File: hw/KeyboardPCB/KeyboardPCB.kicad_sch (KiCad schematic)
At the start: 176 parts, among them IC1 TPS2113ADRBR, IC2 BGM220PC22HNA2R, J1 USB_B_Micro, J2 Conn_01x05_Pin, J3 Conn_01x06_Pin, K1 KEYSW, K10 KEYSW, K11 KEYSW, K12 KEYSW, K13 KEYSW, K14 KEYSW, K15 KEYSW, K16 KEYSW, K17 KEYSW, K18 KEYSW, K19 KEYSW, K2 KEYSW, K21 KEYSW, K22 KEYSW, K23 KEYSW, K24 KEYSW, K26 KEYSW, K27 KEYSW, K28 KEYSW, K29 KEYSW, K3 KEYSW, K30 KEYSW, K31 KEYSW, K32 KEYSW, K33 KEYSW, K34 KEYSW, K36 KEYSW, K37 KEYSW, K38 KEYSW, K39 KEYSW, K4 KEYSW, K41 KEYSW, K42 KEYSW, K43 KEYSW, K44 KEYSW, K46 KEYSW, K47 KEYSW, K48 KEYSW, K49 KEYSW, K5 KEYSW, K50 KEYSW, K51 KEYSW, K52 KEYSW, K53 KEYSW, K54 KEYSW, K55 KEYSW, K56 KEYSW, K57 KEYSW, K58 KEYSW, K59 KEYSW, K6 KEYSW, K60 KEYSW, K61 KEYSW, K62 KEYSW, K64 KEYSW, K65 KEYSW, K66 KEYSW, K67 KEYSW, K68 KEYSW, K69 KEYSW, K7 KEYSW, K8 KEYSW, SW1 SW_Push, U1 TM4C123GH6PMI7, U2 TPS73633DBV, U3 Adafruit ST7735R, X2 16MHz

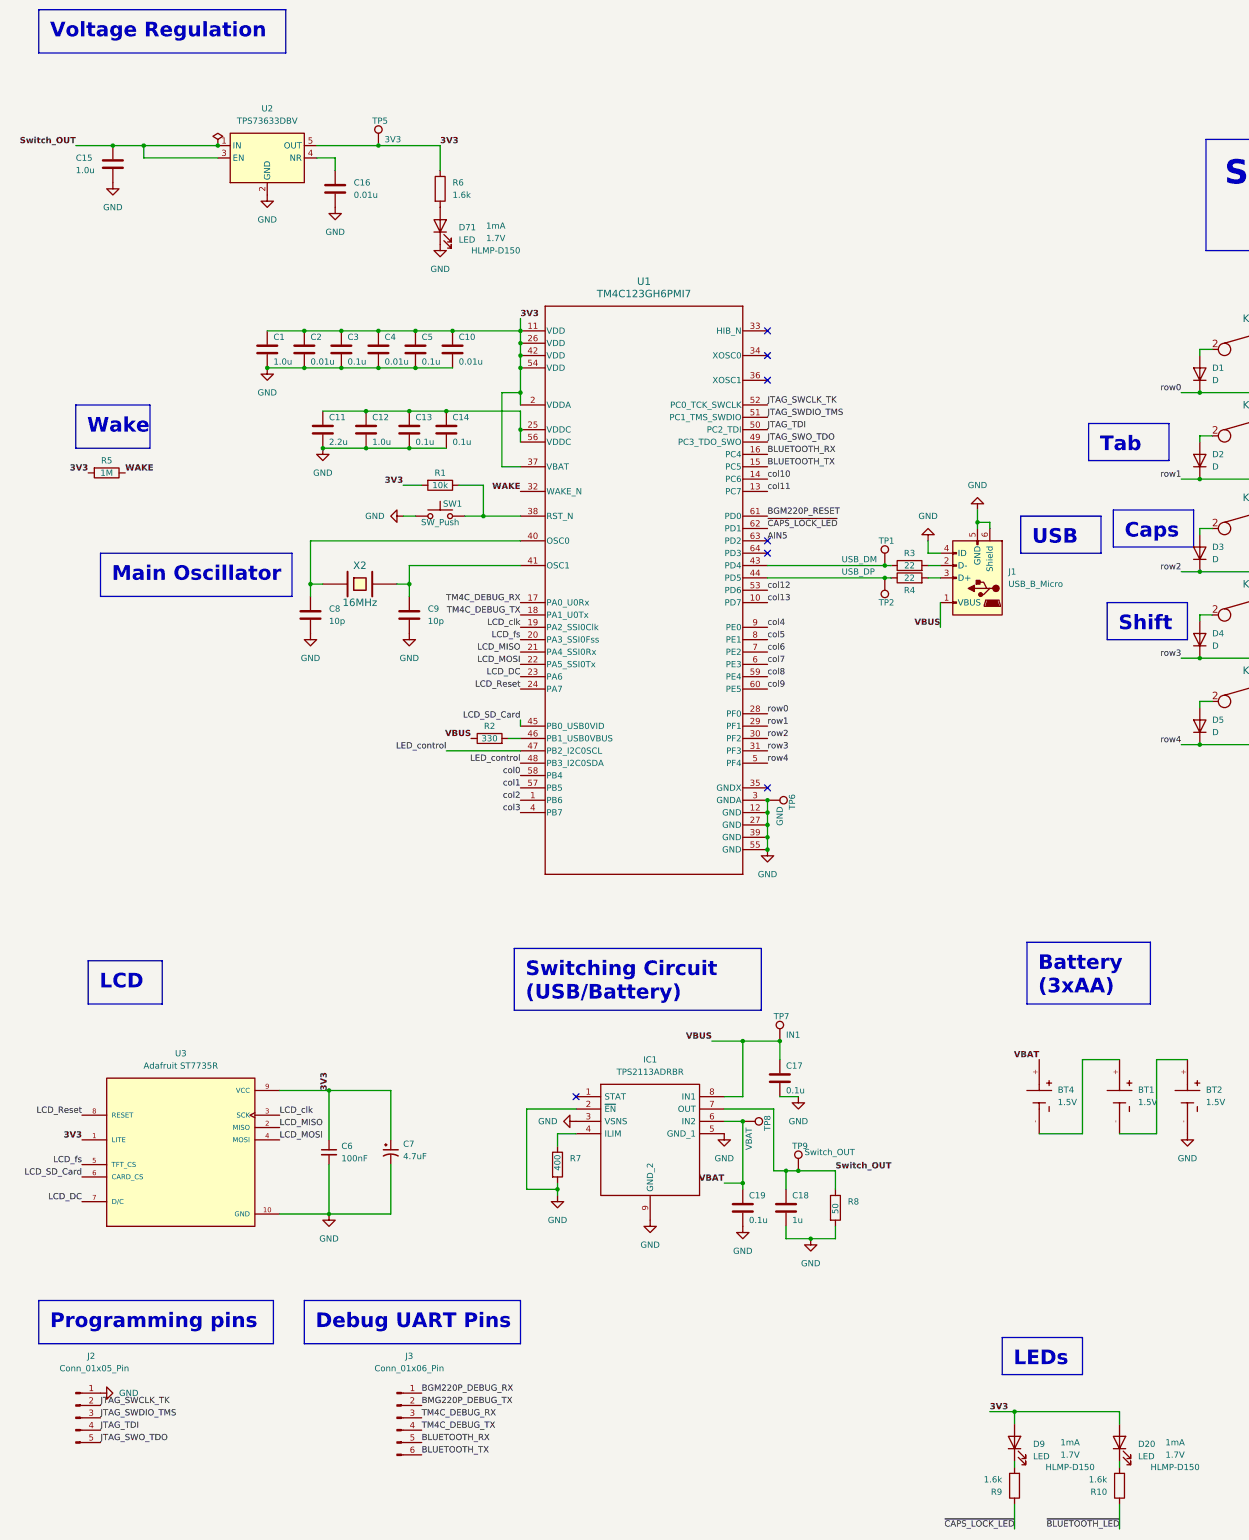
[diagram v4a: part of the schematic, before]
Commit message: Verified TM4C pin #s and important pins, MOSC, and caps
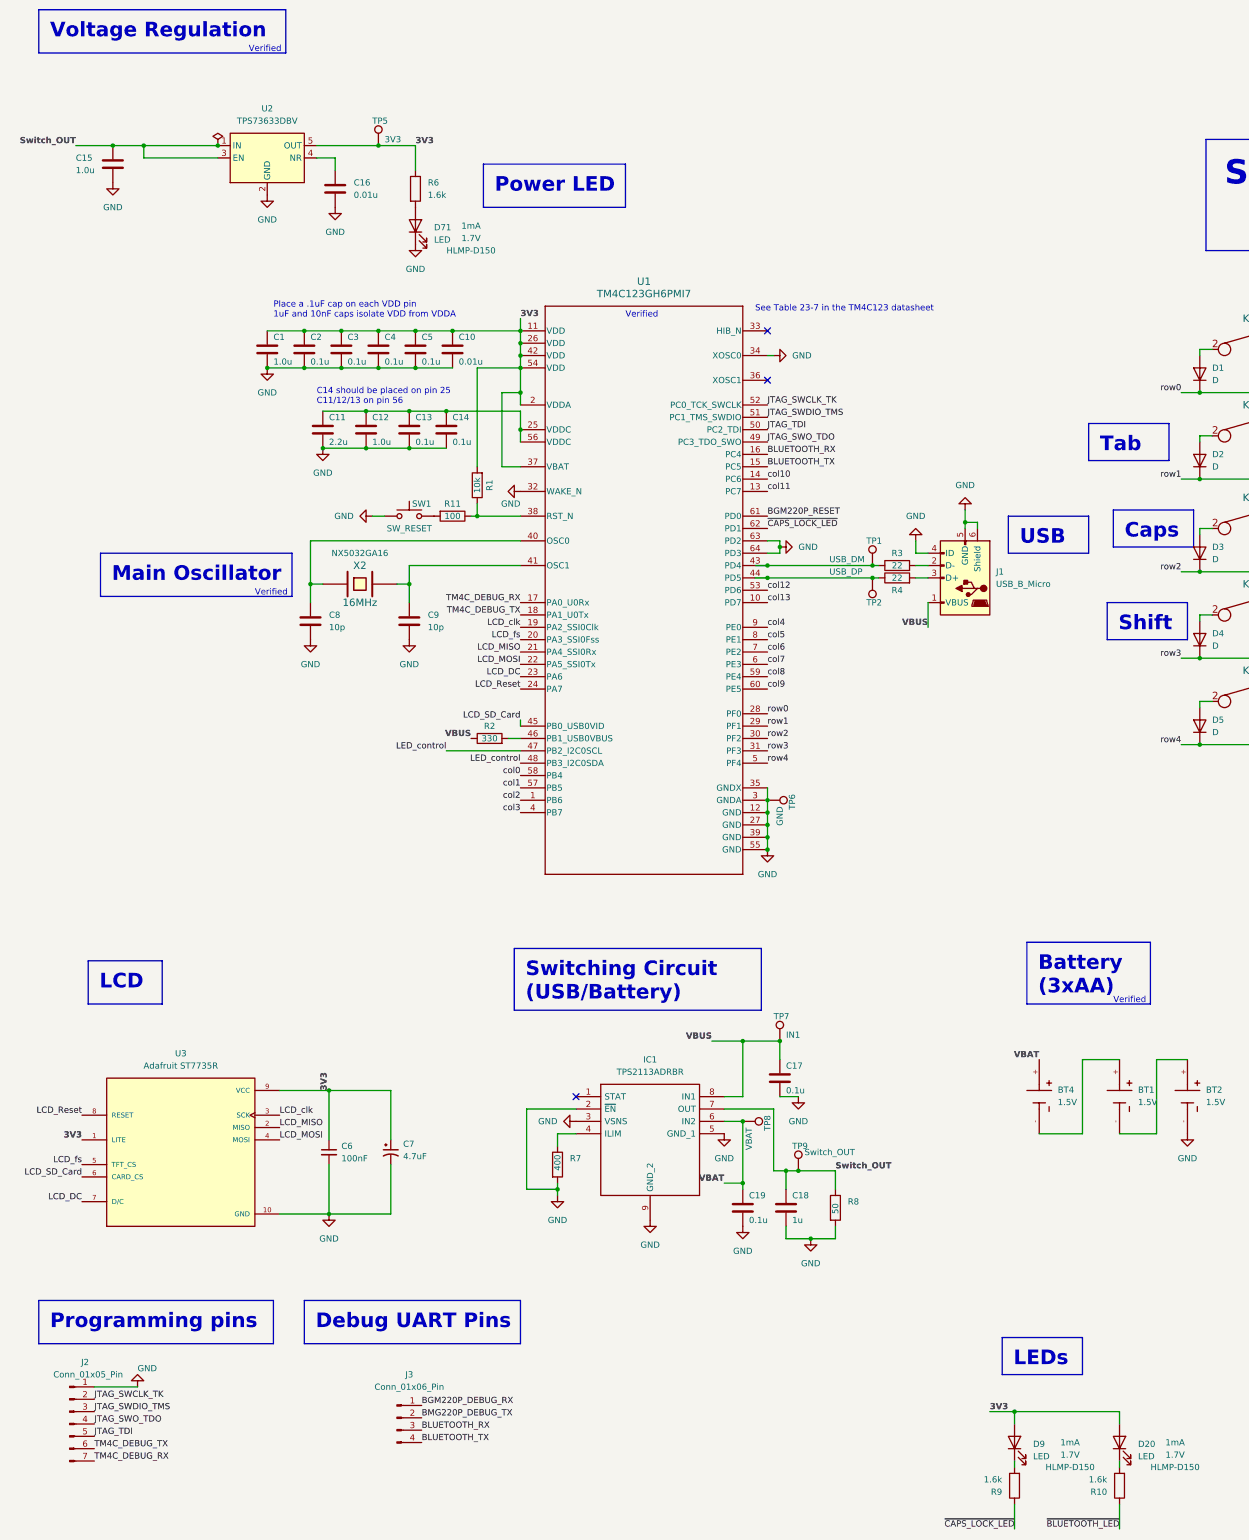
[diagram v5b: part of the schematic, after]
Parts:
- removed R5: 1M, Resistor_SMD:R_0402_1005Metric, symbol Device:R
- added R11: 100, Resistor_SMD:R_0402_1005Metric, symbol Device:R
- C2, C4: value 0.01u -> 0.1u
- J2: symbol Connector:Conn_01x05_Pin -> Connector:Conn_01x07_Pin
- J3: symbol Connector:Conn_01x06_Pin -> Connector:Conn_01x04_Pin
- SW1: value SW_Push -> SW_RESET
- U1: footprint TM4C123GH6PM:PM0064A_L -> TM4C:QFP50P1200X1200X160-64N
- X2: P/N (none) -> NX5032GA16
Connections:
- net AIN5 is gone; now on net GND: U1.63 (PD2)
- net WAKE is gone; now on net GND: U1.32 (WAKE_N)
- net BLUETOOTH_RX: now also J3.3 (Pin_3); no longer J3.5 (Pin_5)
- net BLUETOOTH_TX: now also J3.4 (Pin_4); no longer J3.6 (Pin_6)
- net GND: now also U1.34 (XOSC0), U1.35 (GNDX), U1.64 (PD3)
- net JTAG_SWO_TDO: now also J2.4 (Pin_4); no longer J2.5 (Pin_5)
- net JTAG_TDI: now also J2.5 (Pin_5); no longer J2.4 (Pin_4)
- net TM4C_DEBUG_RX: now also J2.7 (Pin_7); no longer J3.3 (Pin_3)
- net TM4C_DEBUG_TX: now also J2.6 (Pin_6); no longer J3.4 (Pin_4)
- net at R1.1, U1.38 (RST_N): now also R11.1; no longer SW1.2
- new net: R11.2, SW1.2
- no-connect marks 26 -> 22
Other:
- note added: "C14 should be placed on pin 25 C11/12/13 on pin 56"
- note added: "Place a .1uF cap on each VDD pin 1uF and 10nF caps isolate VDD from VDDA"
- note added: "See Table 23-7 in the TM4C123 datasheet"
- note added: "Verified"
- moved on the sheet: C8, C9, D71, J1, R1, R3, R4, R6, SW1, TP1, TP2

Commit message: Verified LCD, power mux, JTAG, USB, and switch matrix
Also changed the switch matrix to use hotswap footprints
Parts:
- removed C18: 1u, Capacitor_SMD:C_0603_1608Metric_Pad1.08x0.95mm_HandSolder, symbol Device:C
- removed R8: 50, Resistor_SMD:R_0402_1005Metric, symbol Device:R
- removed TP9: Switch_OUT, TestPoint:TestPoint_Pad_2.5x2.5mm, symbol Connector:TestPoint
- added TP3: Switch_OUT, TestPoint:TestPoint_Pad_2.5x2.5mm, symbol Connector:TestPoint
- J2: value Conn_01x05_Pin -> Conn_01x07_Pin
- J3: symbol Connector:Conn_01x04_Pin -> Connector:Conn_01x06_Pin
- K1: footprint keebs.pretty-master:Mx_Alps_100 -> MX_Hotswap:MX-Hotswap-1U
- K10: renamed from K46; footprint keebs.pretty-master:Mx_Alps_100 -> MX_Hotswap:MX-Hotswap-1U
- K11: renamed from K51; footprint keebs.pretty-master:Mx_Alps_100 -> MX_Hotswap:MX-Hotswap-1U
- K12: renamed from K56; footprint keebs.pretty-master:Mx_Alps_100 -> MX_Hotswap:MX-Hotswap-1U
- K13: renamed from K61; footprint keebs.pretty-master:Mx_Alps_100 -> MX_Hotswap:MX-Hotswap-1U
- K14: renamed from K66; footprint keebs.pretty-master:Mx_Alps_200 -> MX_Hotswap:MX-Hotswap-2U
- K15: renamed from K2; footprint keebs.pretty-master:Mx_Alps_150 -> MX_Hotswap:MX-Hotswap-1.5U
- K16: renamed from K7; footprint keebs.pretty-master:Mx_Alps_100 -> MX_Hotswap:MX-Hotswap-1U
- K17: renamed from K12; footprint keebs.pretty-master:Mx_Alps_100 -> MX_Hotswap:MX-Hotswap-1U
- K18: renamed from K17; footprint keebs.pretty-master:Mx_Alps_100 -> MX_Hotswap:MX-Hotswap-1U
- K19: renamed from K22; footprint keebs.pretty-master:Mx_Alps_100 -> MX_Hotswap:MX-Hotswap-1U
- K2: renamed from K6; footprint keebs.pretty-master:Mx_Alps_100 -> MX_Hotswap:MX-Hotswap-1U
- K20: renamed from K27; footprint keebs.pretty-master:Mx_Alps_100 -> MX_Hotswap:MX-Hotswap-1U
- K21: renamed from K32; footprint keebs.pretty-master:Mx_Alps_100 -> MX_Hotswap:MX-Hotswap-1U
- K22: renamed from K37; footprint keebs.pretty-master:Mx_Alps_100 -> MX_Hotswap:MX-Hotswap-1U
- K23: renamed from K42; footprint keebs.pretty-master:Mx_Alps_100 -> MX_Hotswap:MX-Hotswap-1U
- K24: renamed from K47; footprint keebs.pretty-master:Mx_Alps_100 -> MX_Hotswap:MX-Hotswap-1U
- K25: renamed from K52; footprint keebs.pretty-master:Mx_Alps_100 -> MX_Hotswap:MX-Hotswap-1U
- K26: renamed from K57; footprint keebs.pretty-master:Mx_Alps_100 -> MX_Hotswap:MX-Hotswap-1U
- K27: renamed from K62; footprint keebs.pretty-master:Mx_Alps_100 -> MX_Hotswap:MX-Hotswap-1U
- K28: renamed from K67; footprint keebs.pretty-master:Mx_Alps_150 -> MX_Hotswap:MX-Hotswap-1.5U
- K29: renamed from K3; footprint keebs.pretty-master:Mx_Alps_175 -> MX_Hotswap:MX-Hotswap-1.75U
- K3: renamed from K11; footprint keebs.pretty-master:Mx_Alps_100 -> MX_Hotswap:MX-Hotswap-1U
- K30: renamed from K8; footprint keebs.pretty-master:Mx_Alps_100 -> MX_Hotswap:MX-Hotswap-1U
- K31: renamed from K13; footprint keebs.pretty-master:Mx_Alps_100 -> MX_Hotswap:MX-Hotswap-1U
- K32: renamed from K18; footprint keebs.pretty-master:Mx_Alps_100 -> MX_Hotswap:MX-Hotswap-1U
- K33: renamed from K23; footprint keebs.pretty-master:Mx_Alps_100 -> MX_Hotswap:MX-Hotswap-1U
- K34: renamed from K28; footprint keebs.pretty-master:Mx_Alps_100 -> MX_Hotswap:MX-Hotswap-1U
- K35: renamed from K33; footprint keebs.pretty-master:Mx_Alps_100 -> MX_Hotswap:MX-Hotswap-1U
- K36: renamed from K38; footprint keebs.pretty-master:Mx_Alps_100 -> MX_Hotswap:MX-Hotswap-1U
- K37: renamed from K43; footprint keebs.pretty-master:Mx_Alps_100 -> MX_Hotswap:MX-Hotswap-1U
- K38: renamed from K48; footprint keebs.pretty-master:Mx_Alps_100 -> MX_Hotswap:MX-Hotswap-1U
- K39: renamed from K53; footprint keebs.pretty-master:Mx_Alps_100 -> MX_Hotswap:MX-Hotswap-1U
- K4: renamed from K16; footprint keebs.pretty-master:Mx_Alps_100 -> MX_Hotswap:MX-Hotswap-1U
- K40: renamed from K58; footprint keebs.pretty-master:Mx_Alps_100 -> MX_Hotswap:MX-Hotswap-1U
- K41: renamed from K68; footprint keebs.pretty-master:Mx_Alps_225 -> MX_Hotswap:MX-Hotswap-2.25U
- K42: renamed from K4; footprint keebs.pretty-master:Mx_Alps_225 -> MX_Hotswap:MX-Hotswap-2.25U
- K43: renamed from K14; footprint keebs.pretty-master:Mx_Alps_100 -> MX_Hotswap:MX-Hotswap-1U
- K44: renamed from K19; footprint keebs.pretty-master:Mx_Alps_100 -> MX_Hotswap:MX-Hotswap-1U
- K45: renamed from K24; footprint keebs.pretty-master:Mx_Alps_100 -> MX_Hotswap:MX-Hotswap-1U
- K46: renamed from K29; footprint keebs.pretty-master:Mx_Alps_100 -> MX_Hotswap:MX-Hotswap-1U
- K47: renamed from K34; footprint keebs.pretty-master:Mx_Alps_100 -> MX_Hotswap:MX-Hotswap-1U
- K48: renamed from K39; footprint keebs.pretty-master:Mx_Alps_100 -> MX_Hotswap:MX-Hotswap-1U
- K49: renamed from K44; footprint keebs.pretty-master:Mx_Alps_100 -> MX_Hotswap:MX-Hotswap-1U
- K5: renamed from K21; footprint keebs.pretty-master:Mx_Alps_100 -> MX_Hotswap:MX-Hotswap-1U
- K50: renamed from K49; footprint keebs.pretty-master:Mx_Alps_100 -> MX_Hotswap:MX-Hotswap-1U
- K51: renamed from K54; footprint keebs.pretty-master:Mx_Alps_100 -> MX_Hotswap:MX-Hotswap-1U
- K52: renamed from K59; footprint keebs.pretty-master:Mx_Alps_100 -> MX_Hotswap:MX-Hotswap-1U
- K53: renamed from K64; footprint keebs.pretty-master:Mx_Alps_150 -> MX_Hotswap:MX-Hotswap-1.5U
- K54: renamed from K69; footprint keebs.pretty-master:Mx_Alps_125 -> MX_Hotswap:MX-Hotswap-1.25U
- K55: renamed from K5; footprint keebs.pretty-master:Mx_Alps_125 -> MX_Hotswap:MX-Hotswap-1.25U
- K56: renamed from K10; footprint keebs.pretty-master:Mx_Alps_125 -> MX_Hotswap:MX-Hotswap-1.25U
- K57: renamed from K15; footprint keebs.pretty-master:Mx_Alps_125 -> MX_Hotswap:MX-Hotswap-1.25U
- K58: renamed from K30; footprint keebs.pretty-master:Mx_Alps_625 -> MX_Hotswap:MX-Hotswap-6.25U
- K59: renamed from K50; footprint keebs.pretty-master:Mx_Alps_125 -> MX_Hotswap:MX-Hotswap-1.25U
- K6: renamed from K26; footprint keebs.pretty-master:Mx_Alps_100 -> MX_Hotswap:MX-Hotswap-1U
- K60: renamed from K55; footprint keebs.pretty-master:Mx_Alps_125 -> MX_Hotswap:MX-Hotswap-1.25U
- K61: renamed from K60; footprint keebs.pretty-master:Mx_Alps_125 -> MX_Hotswap:MX-Hotswap-1.25U
- K62: renamed from K65; footprint keebs.pretty-master:Mx_Alps_125 -> MX_Hotswap:MX-Hotswap-1.25U
- K7: renamed from K31; footprint keebs.pretty-master:Mx_Alps_100 -> MX_Hotswap:MX-Hotswap-1U
- K8: renamed from K36; footprint keebs.pretty-master:Mx_Alps_100 -> MX_Hotswap:MX-Hotswap-1U
- K9: renamed from K41; footprint keebs.pretty-master:Mx_Alps_100 -> MX_Hotswap:MX-Hotswap-1U
- R7: value 400 -> 750
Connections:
- net 3V3: now also J2.5 (Pin_5)
- net GND: now also J2.7 (Pin_7); no longer J1.4 (ID), J2.1 (Pin_1)
- net JTAG_SWDIO_TMS: now also J2.2 (Pin_2); no longer J2.3 (Pin_3)
- net JTAG_SWO_TDO: now also J2.3 (Pin_3); no longer J2.4 (Pin_4)
- net JTAG_TDI: now also J2.4 (Pin_4); no longer J2.5 (Pin_5)
- net Switch_OUT: now also TP3.1
- net TM4C_DEBUG_RX: now also J3.6 (Pin_6); no longer J2.7 (Pin_7)
- net TM4C_DEBUG_TX: now also J3.5 (Pin_5); no longer J2.6 (Pin_6)
- net row0: now also D1.2 (A), D11.2 (A), D16.2 (A), D21.2 (A), D26.2 (A), D31.2 (A), D36.2 (A), D41.2 (A), D46.2 (A), D51.2 (A), D56.2 (A), D6.2 (A), D61.2 (A), D66.2 (A); no longer D1.1 (K), D11.1 (K), D16.1 (K), D21.1 (K), D26.1 (K), D31.1 (K), D36.1 (K), D41.1 (K), D46.1 (K), D51.1 (K), D56.1 (K), D6.1 (K), D61.1 (K), D66.1 (K)
- net row1: now also D12.2 (A), D17.2 (A), D2.2 (A), D22.2 (A), D27.2 (A), D32.2 (A), D37.2 (A), D42.2 (A), D47.2 (A), D52.2 (A), D57.2 (A), D62.2 (A), D67.2 (A), D7.2 (A); no longer D12.1 (K), D17.1 (K), D2.1 (K), D22.1 (K), D27.1 (K), D32.1 (K), D37.1 (K), D42.1 (K), D47.1 (K), D52.1 (K), D57.1 (K), D62.1 (K), D67.1 (K), D7.1 (K)
- net row2: now also D13.2 (A), D18.2 (A), D23.2 (A), D28.2 (A), D3.2 (A), D33.2 (A), D38.2 (A), D43.2 (A), D48.2 (A), D53.2 (A), D58.2 (A), D68.2 (A), D8.2 (A); no longer D13.1 (K), D18.1 (K), D23.1 (K), D28.1 (K), D3.1 (K), D33.1 (K), D38.1 (K), D43.1 (K), D48.1 (K), D53.1 (K), D58.1 (K), D68.1 (K), D8.1 (K)
- net row3: now also D14.2 (A), D19.2 (A), D24.2 (A), D29.2 (A), D34.2 (A), D39.2 (A), D4.2 (A), D44.2 (A), D49.2 (A), D54.2 (A), D59.2 (A), D64.2 (A), D69.2 (A); no longer D14.1 (K), D19.1 (K), D24.1 (K), D29.1 (K), D34.1 (K), D39.1 (K), D4.1 (K), D44.1 (K), D49.1 (K), D54.1 (K), D59.1 (K), D64.1 (K), D69.1 (K)
- net row4: now also D10.2 (A), D15.2 (A), D30.2 (A), D5.2 (A), D50.2 (A), D55.2 (A), D60.2 (A), D65.2 (A); no longer D10.1 (K), D15.1 (K), D30.1 (K), D5.1 (K), D50.1 (K), D55.1 (K), D60.1 (K), D65.1 (K)
- net at K51.2: now also D54.1 (K); no longer D54.2 (A)
- net at K11.2: now also D51.1 (K); no longer D51.2 (A)
- net at K8.2: now also D36.1 (K); no longer D36.2 (A)
- net at K7.2: now also D31.1 (K); no longer D31.2 (A)
- net at K18.2: now also D17.1 (K); no longer D17.2 (A)
- net at K30.2: now also D8.1 (K); no longer D8.2 (A)
- net at K61.2: now also D60.1 (K); no longer D60.2 (A)
- net at K59.2: now also D50.1 (K); no longer D50.2 (A)
- net at K27.2: now also D62.1 (K); no longer D62.2 (A)
- net at K21.2: now also D32.1 (K); no longer D32.2 (A)
- net at K40.2: now also D58.1 (K); no longer D58.2 (A)
- net at K2.2: now also D6.1 (K); no longer D6.2 (A)
- net at K17.2: now also D12.1 (K); no longer D12.2 (A)
- net at K20.2: now also D27.1 (K); no longer D27.2 (A)
- net at K49.2: now also D44.1 (K); no longer D44.2 (A)
- net at K48.2: now also D39.1 (K); no longer D39.2 (A)
- net at K54.2: now also D69.1 (K); no longer D69.2 (A)
- net at K10.2: now also D46.1 (K); no longer D46.2 (A)
- net at K52.2: now also D59.1 (K); no longer D59.2 (A)
- net at K58.2: now also D30.1 (K); no longer D30.2 (A)
- net at K36.2: now also D38.1 (K); no longer D38.2 (A)
- net at K4.2: now also D16.1 (K); no longer D16.2 (A)
- net at K31.2: now also D13.1 (K); no longer D13.2 (A)
- net at K57.2: now also D15.1 (K); no longer D15.2 (A)
- net at K37.2: now also D43.1 (K); no longer D43.2 (A)
- net at K1.2: now also D1.1 (K); no longer D1.2 (A)
- net at K56.2: now also D10.1 (K); no longer D10.2 (A)
- net at K9.2: now also D41.1 (K); no longer D41.2 (A)
- net at K62.2: now also D65.1 (K); no longer D65.2 (A)
- net at K42.2: now also D4.1 (K); no longer D4.2 (A)
- net at K33.2: now also D23.1 (K); no longer D23.2 (A)
- net at K41.2: now also D68.1 (K); no longer D68.2 (A)
- net at K28.2: now also D67.1 (K); no longer D67.2 (A)
- net at K35.2: now also D33.1 (K); no longer D33.2 (A)
- net at K55.2: now also D5.1 (K); no longer D5.2 (A)
- net at K43.2: now also D14.1 (K); no longer D14.2 (A)
- net at K14.2: now also D66.1 (K); no longer D66.2 (A)
- net at K44.2: now also D19.1 (K); no longer D19.2 (A)
- net at K3.2: now also D11.1 (K); no longer D11.2 (A)
- net at K26.2: now also D57.1 (K); no longer D57.2 (A)
- net at K25.2: now also D52.1 (K); no longer D52.2 (A)
- net at K19.2: now also D22.1 (K); no longer D22.2 (A)
- net at K15.2: now also D2.1 (K); no longer D2.2 (A)
- net at K53.2: now also D64.1 (K); no longer D64.2 (A)
- net at K47.2: now also D34.1 (K); no longer D34.2 (A)
- net at K46.2: now also D29.1 (K); no longer D29.2 (A)
- net at K60.2: now also D55.1 (K); no longer D55.2 (A)
- net at K12.2: now also D56.1 (K); no longer D56.2 (A)
- net at K32.2: now also D18.1 (K); no longer D18.2 (A)
- net at K45.2: now also D24.1 (K); no longer D24.2 (A)
- net at K39.2: now also D53.1 (K); no longer D53.2 (A)
- net at K6.2: now also D26.1 (K); no longer D26.2 (A)
- net at K50.2: now also D49.1 (K); no longer D49.2 (A)
- net at K16.2: now also D7.1 (K); no longer D7.2 (A)
- net at K13.2: now also D61.1 (K); no longer D61.2 (A)
- net at K5.2: now also D21.1 (K); no longer D21.2 (A)
- net at K22.2: now also D37.1 (K); no longer D37.2 (A)
- net at K24.2: now also D47.1 (K); no longer D47.2 (A)
- net at K38.2: now also D48.1 (K); no longer D48.2 (A)
- net ~{RESET}: now reaches R1.1, R11.1, U1.38 (RST_N)
- net ~{RESET}: now also J2.6 (Pin_6)
- net at K34.2: now also D28.1 (K); no longer D28.2 (A)
- net at K23.2: now also D42.1 (K); no longer D42.2 (A)
- net at K29.2: now also D3.1 (K); no longer D3.2 (A)
- net JTAG_SWCLK_TK renamed JTAG_SWCLK_TCLK
- net JTAG_SWCLK_TCLK: now also J2.1 (Pin_1); no longer J2.2 (Pin_2)
- no-connect marks 22 -> 23
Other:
- note added: "Already pulled by ICDI TM4C"
- note added: "ID Grounded = HOST ID Floating = DEVICE"
- note added: "ILIM - Current Limit Current Limit = 500/R TPS2113A can do 630mA min limit R = 500/0.630 ~= 800 Ohm"
- note added: "Must have a large copper ground pour to dissipate heat properly"
- note added: "See 24.9.5 in the datasheet"
- note added: "USB series resistors are ??? ripped from an example KB schematic probably just need to ensure 90 ohm diff impedance"
- note added: "only uses like 3mA btw OMEGALUL"
- note added: "who needs a JTAG header?"
- moved on the sheet: C17, C19, D1, D10, D11, D12, D13, D14, D15, D16, D17, D18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

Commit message: Pray to your ECE god of choice
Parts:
- removed R11: 100, Resistor_SMD:R_0402_1005Metric, symbol Device:R
- removed SW1: SW_RESET, Button_Switch_THT:SW_PUSH_6mm, symbol Switch:SW_Push
- added J4: Conn_02x05_Odd_Even, Connector_PinHeader_1.27mm:PinHeader_2x05_P1.27mm_Vertical, symbol Connector_Generic:Conn_02x05_Odd_Even
- added J5: BATT_POS, Connector_Pin:Pin_D1.0mm_L10.0mm, symbol Connector:Conn_01x01_Pin
- added J6: BATT_NEG, Connector_Pin:Pin_D1.0mm_L10.0mm, symbol Connector:Conn_01x01_Pin
- added SW2: BAT_SWITCH, SLW-121586-5A-D:SLW1215865AD, symbol Switch:SW_SPDT
- BT1, BT2, BT4: footprint BA1AAPC:BAT_BA1AAPC -> (none)
- C6: value 100nF -> 0.1uF
- C8, C9: Tolerance (none) -> <5%
- D1, D10, D11, D12, D13, D14, D15, D16, D17, D18, D19, D2, D21, D22, D23, D24, D26, D27, D28, D29, D3, D30, D31, D32, D33, D34, D36, D37, D38, D39, D4, D41, D42, D43, D44, D46, D47, D48, D49, D5, D50, D51, D52, D53, D54, D55, D56, D57, D58, D59, D6, D60, D61, D62, D64, D65, D66, D67, D68, D69, D7, D8: footprint Diode_SMD:D_0603_1608Metric_Pad1.05x0.95mm_HandSolder -> Diode_SMD:D_SOD-123
- J2: footprint Connector_PinHeader_2.54mm:PinHeader_1x05_P2.54mm_Vertical -> Connector_PinHeader_2.54mm:PinHeader_1x07_P2.54mm_Vertical
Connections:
- net 3V3: now also J4.1 (Pin_1)
- net GND: now also U1.61 (PD0), J4.2 (Pin_2), J6.1 (Pin_1), SW2.3 (C)
- net VBAT: now also SW2.2 (B); no longer BT4.+
- net ~{RESET}: now also IC2.30 (RESETN), J4.3 (Pin_3)
- net BGM_SWO: now reaches IC2.10 (PA03)
- net BGM_SWO: now also J4.6 (Pin_6)
- net PTI_DOUT: now reaches IC2.26 (PC04)
- net PTI_DOUT: now also J4.10 (Pin_10)
- net PTI_DFRAME: now reaches IC2.27 (PC05)
- net PTI_DFRAME: now also J4.9 (Pin_9)
- net BGM_SWCLK: now reaches IC2.8 (PA01)
- net BGM_SWCLK: now also J4.8 (Pin_8)
- net BGM_SWDIO: now reaches IC2.9 (PA02)
- net BGM_SWDIO: now also J4.7 (Pin_7)
- removed net BGM220P_RESET: IC2.30 (RESETN), U1.61 (PD0)
- new net: BT4.+, J5.1 (Pin_1), SW2.1 (A)
- no-connect marks 23 -> 20
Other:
- note added: "No reset switch necessary Just toggle the power (switch or JTAG)"
